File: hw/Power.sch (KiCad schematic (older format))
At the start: 11 parts, among them U6 LM2597, U7 MCP1703T_3V3

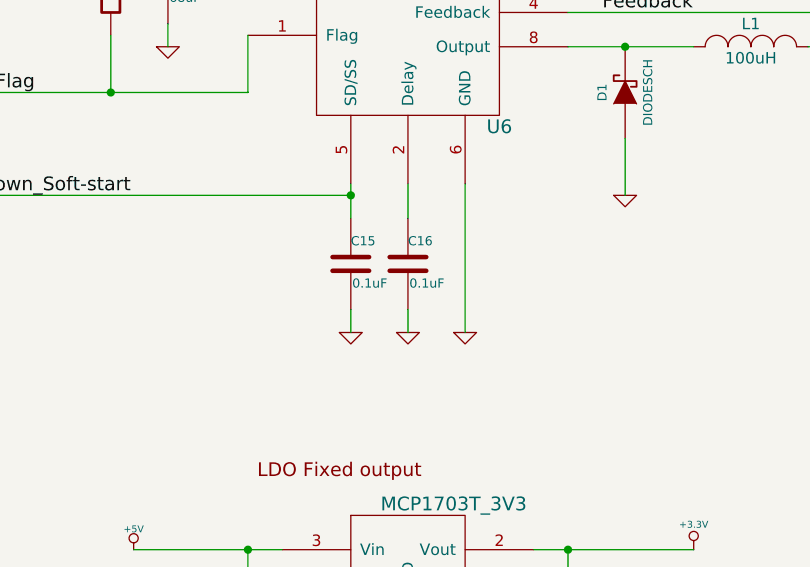
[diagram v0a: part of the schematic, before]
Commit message: Added additional caps to the DAC on the stepper feedback
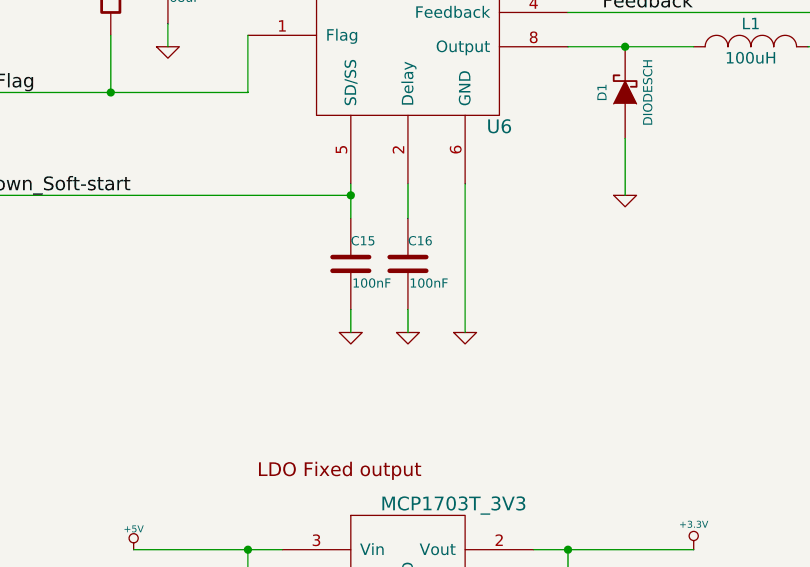
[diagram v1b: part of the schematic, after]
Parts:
- C15, C16: value 0.1uF -> 100nF
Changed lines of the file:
@@
 P 5300 3750
 F 0 "C15" H 5300 3850 40  0000 L CNN
-F 1 "0.1uF" H 5306 3665 40  0000 L CNN
+F 1 "100nF" H 5306 3665 40  0000 L CNN
 F 2 "" H 5338 3600 30  0000 C CNN
 F 3 "" H 5300 3750 60  0000 C CNN
@@
 P 5550 3750
 F 0 "C16" H 5550 3850 40  0000 L CNN
-F 1 "0.1uF" H 5556 3665 40  0000 L CNN
+F 1 "100nF" H 5556 3665 40  0000 L CNN
 F 2 "" H 5588 3600 30  0000 C CNN
 F 3 "" H 5550 3750 60  0000 C CNN
@@
 	5800 3400 5800 4050
 $Comp
-L GND #PWR035
+L GND #PWR038
 U 1 1 538BA3AF
 P 4500 2800
-F 0 "#PWR035" H 4500 2800 30  0001 C CNN
+F 0 "#PWR038" H 4500 2800 30  0001 C CNN
 F 1 "GND" H 4500 2730 30  0001 C CNN
 F 2 "" H 4500 2800 60  0000 C CNN
@@
 $EndComp
 $Comp
-L GND #PWR036
+L GND #PWR039
 U 1 1 538BA3C3
 P 5300 4050
-F 0 "#PWR036" H 5300 4050 30  0001 C CNN
+F 0 "#PWR039" H 5300 4050 30  0001 C CNN
 F 1 "GND" H 5300 3980 30  0001 C CNN
 F 2 "" H 5300 4050 60  0000 C CNN
@@
 $EndComp
 $Comp
-L GND #PWR037
+L GND #PWR040
 U 1 1 538BA3D7
 P 5550 4050
-F 0 "#PWR037" H 5550 4050 30  0001 C CNN
+F 0 "#PWR040" H 5550 4050 30  0001 C CNN
 F 1 "GND" H 5550 3980 30  0001 C CNN
 F 2 "" H 5550 4050 60  0000 C CNN
@@
 $EndComp
 $Comp
-L GND #PWR038
+L GND #PWR041
 U 1 1 538BA3EB
 P 5800 4050
-F 0 "#PWR038" H 5800 4050 30  0001 C CNN
+F 0 "#PWR041" H 5800 4050 30  0001 C CNN
 F 1 "GND" H 5800 3980 30  0001 C CNN
 F 2 "" H 5800 4050 60  0000 C CNN
@@
 $EndComp
 $Comp
-L GND #PWR039
+L GND #PWR042
 U 1 1 538BA43B
 P 7700 3450
-F 0 "#PWR039" H 7700 3450 30  0001 C CNN
+F 0 "#PWR042" H 7700 3450 30  0001 C CNN
 F 1 "GND" H 7700 3380 30  0001 C CNN
 F 2 "" H 7700 3450 60  0000 C CNN
@@
 	7700 3450 7700 3300
 $Comp
-L GND #PWR040
+L GND #PWR043
 U 1 1 538BA4AD
 P 6500 3450
-F 0 "#PWR040" H 6500 3450 30  0001 C CNN
+F 0 "#PWR043" H 6500 3450 30  0001 C CNN
 F 1 "GND" H 6500 3380 30  0001 C CNN
 F 2 "" H 6500 3450 60  0000 C CNN
@@
 $EndComp
 $Comp
-L GND #PWR041
+L GND #PWR044
 U 1 1 539DD74C
 P 5550 5650
-F 0 "#PWR041" H 5550 5650 30  0001 C CNN
+F 0 "#PWR044" H 5550 5650 30  0001 C CNN
 F 1 "GND" H 5550 5580 30  0001 C CNN
 F 2 "" H 5550 5650 60  0000 C CNN
@@
 	4850 5500 4850 5650
 $Comp
-L GND #PWR042
+L GND #PWR045
 U 1 1 539DD760
 P 6250 5650
-F 0 "#PWR042" H 6250 5650 30  0001 C CNN
+F 0 "#PWR045" H 6250 5650 30  0001 C CNN
 F 1 "GND" H 6250 5580 30  0001 C CNN
 F 2 "" H 6250 5650 60  0000 C CNN
@@
 $EndComp
 $Comp
-L GND #PWR043
+L GND #PWR046
 U 1 1 539DD766
 P 4850 5650
-F 0 "#PWR043" H 4850 5650 30  0001 C CNN
+F 0 "#PWR046" H 4850 5650 30  0001 C CNN
 F 1 "GND" H 4850 5580 30  0001 C CNN
 F 2 "" H 4850 5650 60  0000 C CNN
@@
 45V
 $Comp
-L +5V #PWR044
+L +5V #PWR047
 U 1 1 539E2B50
 P 8150 2800
-F 0 "#PWR044" H 8150 2890 20  0001 C CNN
+F 0 "#PWR047" H 8150 2890 20  0001 C CNN
 F 1 "+5V" H 8150 2890 30  0000 C CNN
 F 2 "" H 8150 2800 60  0000 C CNN
@@
 $EndComp
 $Comp
-L +5V #PWR045
+L +5V #PWR048
 U 1 1 539E2B64
 P 4350 5000
-F 0 "#PWR045" H 4350 5090 20  0001 C CNN
+F 0 "#PWR048" H 4350 5090 20  0001 C CNN
 F 1 "+5V" H 4350 5090 30  0000 C CNN
 F 2 "" H 4350 5000 60  0000 C CNN
@@
 $EndComp
 $Comp
-L +3.3V #PWR046
+L +3.3V #PWR049
 U 1 1 539E2B78
 P 6800 5000
-F 0 "#PWR046" H 6800 4960 30  0001 C CNN
+F 0 "#PWR049" H 6800 4960 30  0001 C CNN
 F 1 "+3.3V" H 6800 5110 30  0000 C CNN
 F 2 "" H 6800 5000 60  0000 C CNN
@@
 $EndComp
 $Comp
-L PWR_FLAG #FLG047
+L PWR_FLAG #FLG050
 U 1 1 539E3DBF
 P 8150 2800
-F 0 "#FLG047" H 8150 2895 30  0001 C CNN
+F 0 "#FLG050" H 8150 2895 30  0001 C CNN
 F 1 "PWR_FLAG" H 8150 2980 30  0000 C CNN
 F 2 "" H 8150 2800 60  0000 C CNN
